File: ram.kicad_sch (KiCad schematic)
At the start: 36 parts, among them IC25 74LVC139, U2 TXS0108EPW, U3 TXS0108EPW, U4 TXS0108EPW, U5 TXS0108EPW, U6 IS41LV16105D, U7 IS41LV16105D, U8 TXS0108EPW, U9 TXS0108EPW

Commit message: revise for fabrication
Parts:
- added IC11, IC6: HM514260AJ8, Acorn:SOJ-42_10.16mm_P1.27mm, symbol Acorn:HYB5118165BSJ
- added RP2, RP4, RP5, RP6: 68R, Package_SO:SOIC-16W_5.3x10.2mm_P1.27mm, symbol Device:R_Pack08
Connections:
- net +3.3V: now also C152.1, C160.1, C163.1, C166.1, C2.1, C4.1; no longer C11.1, C12.1, C13.1, C131.1, C162.2, C17.1, C18.1, C19.1, C228.1, IC25.13 (A1), IC25.14 (A0), IC25.15 (E), IC25.16 (VCC), L15.1, L16.1, R136.1
- net +5V: now also C11.1, C12.1, C13.1, C131.1, C162.2, C17.1, C18.1, C19.1, C228.1, IC25.13 (A1), IC25.14 (A0), IC25.15 (E), IC25.16 (VCC), L15.1, L16.1, R136.1, IC11.1 (Vcc), IC11.21 (Vcc), IC11.6 (Vcc), IC6.1 (Vcc), IC6.21 (Vcc), IC6.6 (Vcc); no longer C152.1, C160.1, C163.1, C166.1, C2.1, C4.1
- net Cas0: now also IC6.31 (~{LCAS})
- net Cas1: now also IC6.30 (~{UCAS})
- net Cas2: now also IC11.31 (~{LCAS})
- net Cas3: now also IC11.30 (~{UCAS})
- net D0: now also RP2.1 (R1.1)
- net D1: now also RP2.2 (R2.1)
- net D10: now also RP4.6 (R6.1)
- net D11: now also RP4.5 (R5.1)
- net D12: now also RP4.4 (R4.1)
- net D13: now also RP4.3 (R3.1)
- net D14: now also RP4.2 (R2.1)
- net D15: now also RP4.1 (R1.1)
- net D16: now also RP5.8 (R8.1)
- net D17: now also RP5.7 (R7.1)
- net D18: now also RP5.6 (R6.1)
- net D19: now also RP5.5 (R5.1)
- net D2: now also RP2.3 (R3.1)
- net D20: now also RP5.4 (R4.1)
- net D21: now also RP5.3 (R3.1)
- net D22: now also RP5.2 (R2.1)
- net D23: now also RP5.1 (R1.1)
- net D24: now also RP6.4 (R4.1)
- net D25: now also RP6.3 (R3.1)
- net D26: now also RP6.2 (R2.1)
- net D27: now also RP6.1 (R1.1)
- net D28: now also RP6.5 (R5.1)
- net D29: now also RP6.6 (R6.1)
- net D3: now also RP2.4 (R4.1)
- net D30: now also RP6.7 (R7.1)
- net D31: now also RP6.8 (R8.1)
- net D4: now also RP2.5 (R5.1)
- net D5: now also RP2.6 (R6.1)
- net D6: now also RP2.7 (R7.1)
- net D7: now also RP2.8 (R8.1)
- net D8: now also RP4.8 (R8.1)
- net D9: now also RP4.7 (R7.1)
- net Dbe: now also IC25.2 (A0)
- net Dbe3: no longer IC25.2 (A0)
- net GND: now also IC11.22 (Vss), IC11.37 (Vss), IC11.42 (Vss), IC6.22 (Vss), IC6.37 (Vss), IC6.42 (Vss)
- net Ra0: now also IC11.17 (A0), IC6.17 (A0)
- net Ra1: now also IC11.18 (A1), IC6.18 (A1)
- net Ra2: now also IC11.19 (A2), IC6.19 (A2)
- net Ra3: now also IC11.20 (A3), IC6.20 (A3)
- net Ra4: now also IC11.23 (A4), IC6.23 (A4)
- net Ra5: now also IC11.24 (A5), IC6.24 (A5)
- net Ra6: now also IC11.25 (A6), IC6.25 (A6)
- net Ra7: now also IC11.26 (A7), IC6.26 (A7)
- net Ra8: now also IC11.27 (A8), IC6.27 (A8)
- net Ra9: now also IC11.28 (A9), IC6.28 (A9)
- net Rd0: now also IC6.2 (IO0), RP2.16 (R1.2)
- net Rd1: now also IC6.3 (IO1), RP2.15 (R2.2)
- net Rd10: now also IC6.35 (IO10), RP4.11 (R6.2)
- net Rd11: now also IC6.36 (IO11), RP4.12 (R5.2)
- net Rd12: now also IC6.38 (IO12), RP4.13 (R4.2)
- net Rd13: now also IC6.39 (IO13), RP4.14 (R3.2)
- net Rd14: now also IC6.40 (IO14), RP4.15 (R2.2)
- net Rd15: now also IC6.41 (IO15), RP4.16 (R1.2)
- net Rd16: now also IC11.2 (IO0), RP5.9 (R8.2)
- net Rd17: now also IC11.3 (IO1), RP5.10 (R7.2)
- net Rd18: now also IC11.4 (IO2), RP5.11 (R6.2)
- net Rd19: now also IC11.5 (IO3), RP5.12 (R5.2)
- net Rd2: now also IC6.4 (IO2), RP2.14 (R3.2)
- net Rd20: now also IC11.7 (IO4), RP5.13 (R4.2)
- net Rd21: now also IC11.8 (IO5), RP5.14 (R3.2)
- net Rd22: now also IC11.9 (IO6), RP5.15 (R2.2)
- net Rd23: now also IC11.10 (IO7), RP5.16 (R1.2)
- net Rd24: now also IC11.36 (IO11), RP6.13 (R4.2)
- net Rd25: now also IC11.35 (IO10), RP6.14 (R3.2)
- net Rd26: now also IC11.34 (IO9), RP6.15 (R2.2)
- net Rd27: now also IC11.33 (IO8), RP6.16 (R1.2)
- net Rd28: now also IC11.38 (IO12), RP6.12 (R5.2)
- net Rd29: now also IC11.39 (IO13), RP6.11 (R6.2)
- net Rd3: now also IC6.5 (IO3), RP2.13 (R4.2)
- net Rd30: now also IC11.40 (IO14), RP6.10 (R7.2)
- net Rd31: now also IC11.41 (IO15), RP6.9 (R8.2)
- net Rd4: now also IC6.7 (IO4), RP2.12 (R5.2)
- net Rd5: now also IC6.8 (IO5), RP2.11 (R6.2)
- net Rd6: now also IC6.9 (IO6), RP2.10 (R7.2)
- net Rd7: now also IC6.10 (IO7), RP2.9 (R8.2)
- net Rd8: now also IC6.33 (IO8), RP4.9 (R8.2)
- net Rd9: now also IC6.34 (IO9), RP4.10 (R7.2)
- net ~{OE2}: now also IC11.29 (~{OE}), IC6.29 (~{OE})
- net ~{Ras}: now also IC11.14 (~{RAS}), IC6.14 (~{RAS})
- net ~{WR2}: now also IC11.13 (~{WE}), IC6.13 (~{WE})
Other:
- moved on the sheet: U2, U3, U4, U5, U6, U7, U8, U9

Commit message: prepare for fabrication
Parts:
- C10, C11, C12, C13, C152, C160, C162, C163, C166, C17, C18, C19, C2, C4, C5, C6, C7, C8, C9: LCSC (none) -> C49678; LCSC Part (none) -> C49678
- IC25: LCSC (none) -> C7662; LCSC Part (none) -> C7662
- R135: LCSC (none) -> C17630; LCSC Part (none) -> C17630
- R136: LCSC (none) -> C2907219; LCSC Part (none) -> C2907219
- RP2, RP4, RP5, RP6: value 68R -> 68Rx8; LCSC (none) -> C1739978; LCSC Part (none) -> C1739978
- U2, U3, U4, U5, U8, U9: LCSC (none) -> C17206; LCSC Part (none) -> C17206
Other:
- moved on the sheet: RP2, RP4, RP5, RP6

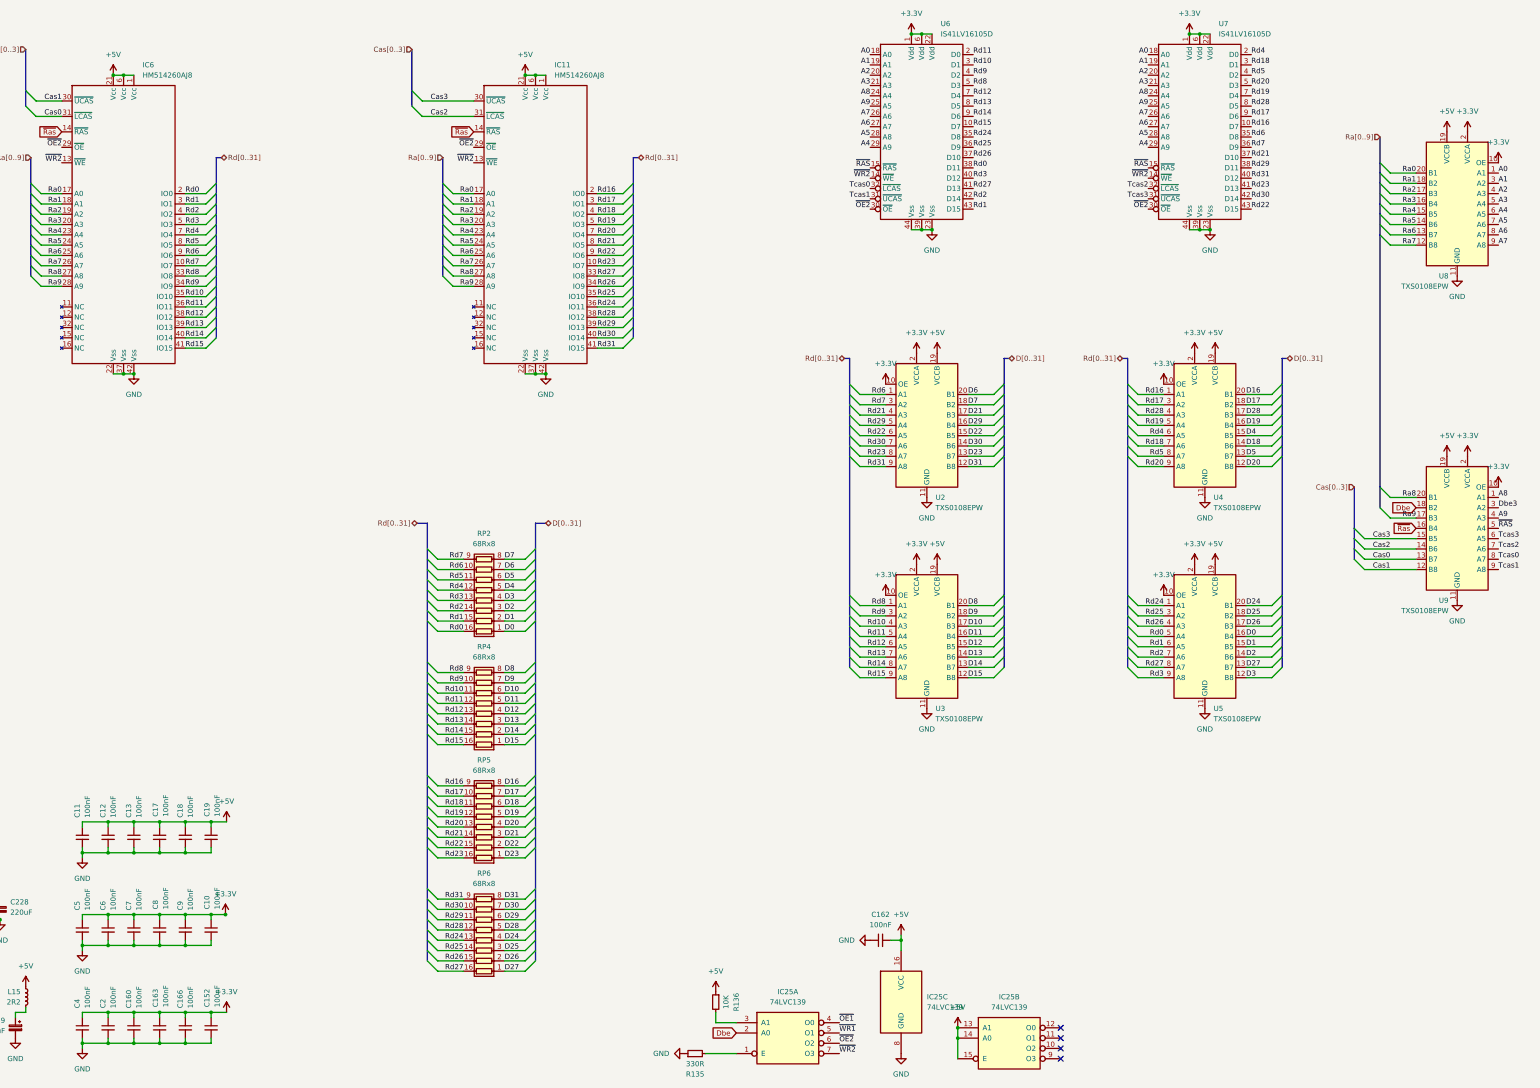
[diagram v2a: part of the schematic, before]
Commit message: fix CX1
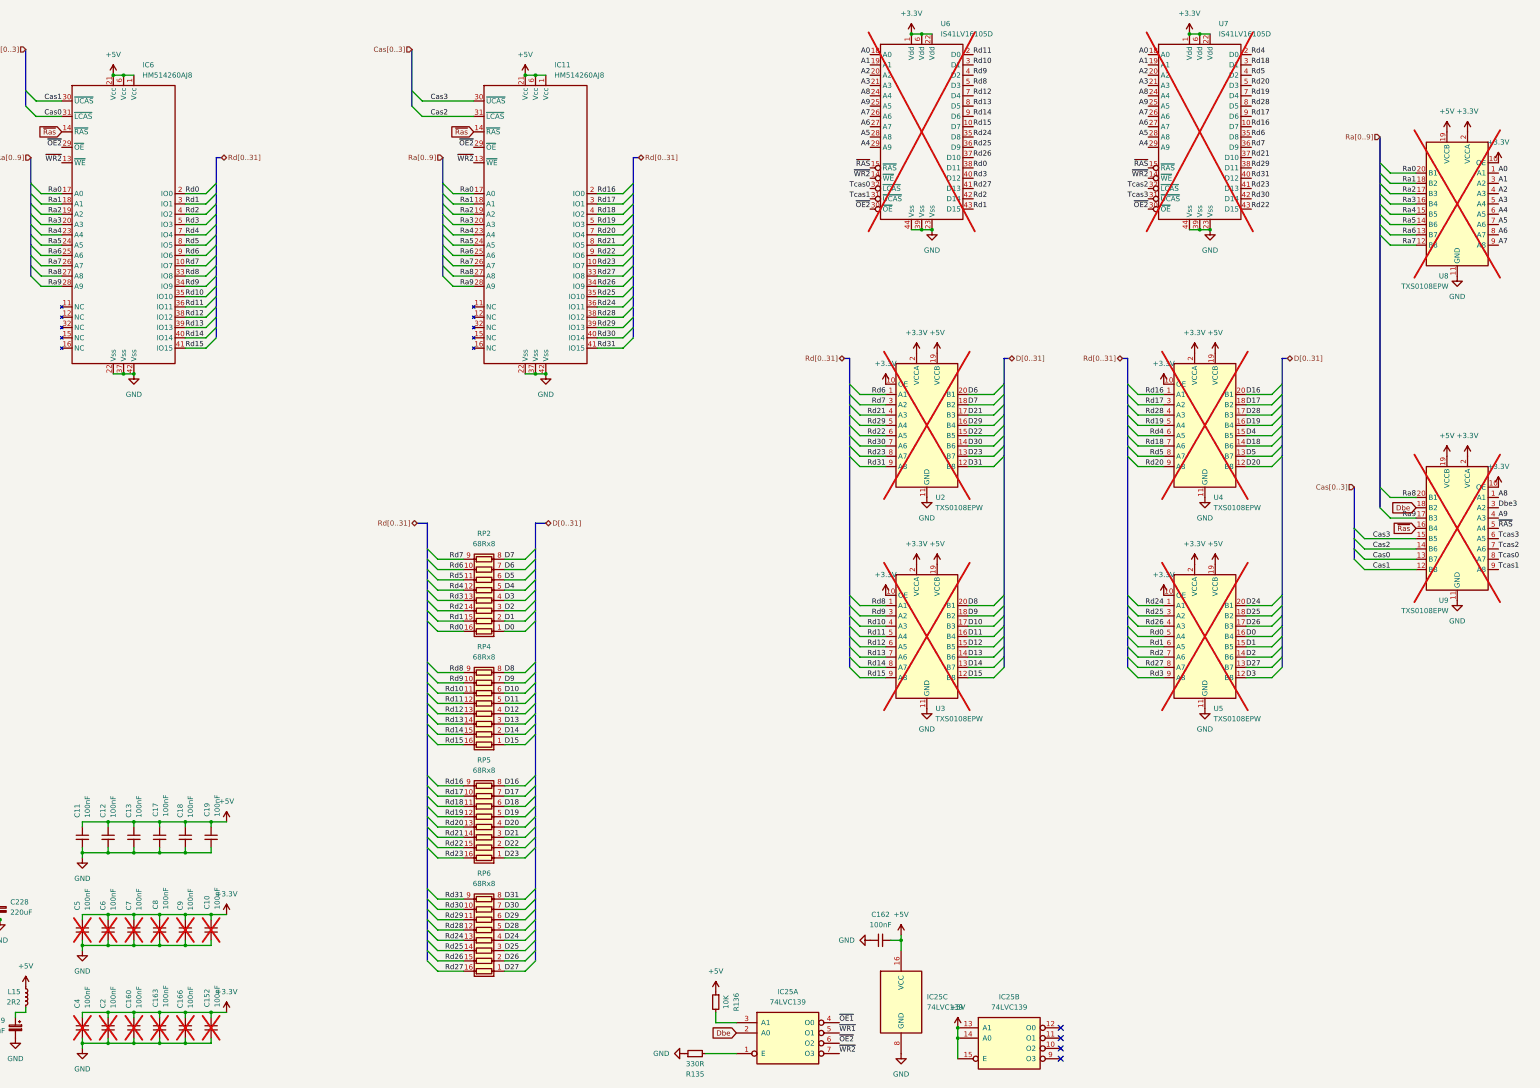
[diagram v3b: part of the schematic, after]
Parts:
- C10, C152, C160, C163, C166, C2, C4, C5, C6, C7, C8, C9, U2, U3, U4, U5, U6, U7, U8, U9: now not fitted; now left out of the parts list
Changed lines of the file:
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@@
 	)
 	(junction
-		(at 84.8234 238.76)
-		(diameter 0)
-		(color 0 0 0 0)
-	)
-	(junction
 		(at 256.54 21.59)
 		(diameter 0)
@@
 	(wire
 		(pts
-			(xy 81.28 238.76) (xy 84.8234 238.76)
+			(xy 81.28 238.76) (xy 85.09 238.76)
 		)
 		(stroke
@@
 	(wire
 		(pts
-			(xy 84.8234 238.76) (xy 85.09 238.76)
-		)
-		(stroke
-			(width 0)
-			(type default)
-		)
-	)
-	(wire
-		(pts
 			(xy 241.3 123.19) (xy 247.65 123.19)
 		)
@@
 		(unit 1)
 		(exclude_from_sim no)
-		(in_bom yes)
+		(in_bom no)
 		(on_board no)
-		(dnp no)
+		(dnp yes)
 		(property "Reference" "C4"
 			(at 48.26 261.874 90)
@@
 		(unit 1)
 		(exclude_from_sim no)
-		(in_bom yes)
+		(in_bom no)
 		(on_board no)
-		(dnp no)
+		(dnp yes)
 		(fields_autoplaced yes)
 		(property "Reference" "U7"
@@
 		(unit 1)
 		(exclude_from_sim no)
-		(in_bom yes)
+		(in_bom no)
 		(on_board no)
-		(dnp no)
+		(dnp yes)
 		(property "Reference" "C5"
 			(at 48.26 237.744 90)
@@
 		(unit 1)
 		(exclude_from_sim no)
-		(in_bom yes)
+		(in_bom no)
 		(on_board no)
-		(dnp no)
+		(dnp yes)
 		(property "Reference" "C152"
 			(at 80.264 261.62 90)
@@
 		(unit 1)
 		(exclude_from_sim no)
-		(in_bom yes)
+		(in_bom no)
 		(on_board no)
-		(dnp no)
+		(dnp yes)
 		(property "Reference" "C10"
 			(at 80.264 237.49 90)
@@
 		(unit 1)
 		(exclude_from_sim no)
-		(in_bom yes)
+		(in_bom no)
 		(on_board no)
-		(dnp no)
+		(dnp yes)
 		(property "Reference" "C6"
 			(at 54.61 237.744 90)
@@
 		(unit 1)
 		(exclude_from_sim no)
-		(in_bom yes)
+		(in_bom no)
 		(on_board no)
-		(dnp no)
+		(dnp yes)
 		(property "Reference" "C163"
 			(at 67.564 261.62 90)
@@
 		(unit 1)
 		(exclude_from_sim no)
-		(in_bom yes)
+		(in_bom no)
 		(on_board no)
-		(dnp no)
+		(dnp yes)
 		(fields_autoplaced yes)
 		(property "Reference" "U8"
@@
 		(unit 1)
 		(exclude_from_sim no)
-		(in_bom yes)
+		(in_bom no)
 		(on_board no)
-		(dnp no)
+		(dnp yes)
 		(fields_autoplaced yes)
 		(property "Reference" "U9"
@@
 		(unit 1)
 		(exclude_from_sim no)
-		(in_bom yes)
+		(in_bom no)
 		(on_board no)
-		(dnp no)
+		(dnp yes)
 		(fields_autoplaced yes)
 		(property "Reference" "U6"
@@
 		(unit 1)
 		(exclude_from_sim no)
-		(in_bom yes)
+		(in_bom no)
 		(on_board no)
-		(dnp no)
+		(dnp yes)
 		(fields_autoplaced yes)
 		(property "Reference" "U3"
@@
 		(unit 1)
 		(exclude_from_sim no)
-		(in_bom yes)
+		(in_bom no)
 		(on_board no)
-		(dnp no)
+		(dnp yes)
 		(property "Reference" "C160"
 			(at 60.96 261.874 90)
@@
 		(unit 1)
 		(exclude_from_sim no)
-		(in_bom yes)
+		(in_bom no)
 		(on_board no)
-		(dnp no)
+		(dnp yes)
 		(property "Reference" "C166"
 			(at 73.66 261.874 90)
@@
 		(unit 1)
 		(exclude_from_sim no)
-		(in_bom yes)
+		(in_bom no)
 		(on_board no)
-		(dnp no)
+		(dnp yes)
 		(fields_autoplaced yes)
 		(property "Reference" "U5"
@@
 		(unit 1)
 		(exclude_from_sim no)
-		(in_bom yes)
+		(in_bom no)
 		(on_board no)
-		(dnp no)
+		(dnp yes)
 		(fields_autoplaced yes)
 		(property "Reference" "U2"
@@
 		(unit 1)
 		(exclude_from_sim no)
-		(in_bom yes)
+		(in_bom no)
 		(on_board no)
-		(dnp no)
+		(dnp yes)
 		(fields_autoplaced yes)
 		(property "Reference" "U4"
@@
 		(unit 1)
 		(exclude_from_sim no)
-		(in_bom yes)
+		(in_bom no)
 		(on_board no)
-		(dnp no)
+		(dnp yes)
 		(property "Reference" "C2"
 			(at 54.61 261.874 90)
@@
 	(symbol
 		(lib_id "power:+3.3V")
-		(at 84.8234 238.76 0)
+		(at 85.09 238.76 0)
 		(unit 1)
 		(exclude_from_sim no)
@@
 		(fields_autoplaced yes)
 		(property "Reference" "#PWR019"
-			(at 84.8234 242.57 0)
+			(at 85.09 242.57 0)
 			(effects
 				(font
@@
 		)
 		(property "Value" "+3.3V"
-			(at 84.8234 233.68 0)
+			(at 85.09 233.68 0)
 			(effects
 				(font
@@
 		)
 		(property "Footprint" ""
-			(at 84.8234 238.76 0)
+			(at 85.09 238.76 0)
 			(effects
 				(font
@@
 		)
 		(property "Datasheet" ""
-			(at 84.8234 238.76 0)
+			(at 85.09 238.76 0)
 			(effects
 				(font
@@
 		)
 		(property "Description" "Power symbol creates a global label with name \"+3.3V\""
-			(at 84.8234 238.76 0)
+			(at 85.09 238.76 0)
 			(effects
 				(font
@@
 		(unit 1)
 		(exclude_from_sim no)
-		(in_bom yes)
+		(in_bom no)
 		(on_board no)
-		(dnp no)
+		(dnp yes)
 		(property "Reference" "C8"
 			(at 67.564 237.49 90)
@@
 		(unit 1)
 		(exclude_from_sim no)
-		(in_bom yes)
+		(in_bom no)
 		(on_board no)
-		(dnp no)
+		(dnp yes)
 		(property "Reference" "C9"
 			(at 73.66 237.744 90)
@@
 		(unit 1)
 		(exclude_from_sim no)
-		(in_bom yes)
+		(in_bom no)
 		(on_board no)
-		(dnp no)
+		(dnp yes)
 		(property "Reference" "C7"
 			(at 60.96 237.744 90)

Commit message: update design to correct errors found by IanJ
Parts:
- IC25: value 74LVC139 -> 74ALS139; footprint Package_SO:TSSOP-16_4.4x5mm_P0.65mm -> Package_SO:SOIC-16_3.9x9.9mm_P1.27mm; LCSC C7662 -> (none); LCSC Part C7662 -> (none)
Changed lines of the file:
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@@
 			)
 		)
-		(property "Value" "74LVC139"
+		(property "Value" "74ALS139"
 			(at 223.52 260.35 0)
 			(effects
@@
 			)
 		)
-		(property "Footprint" "Package_SO:TSSOP-16_4.4x5mm_P0.65mm"
+		(property "Footprint" "Package_SO:SOIC-16_3.9x9.9mm_P1.27mm"
 			(at 223.52 267.97 0)
 			(effects
@@
 			)
 		)
-		(property "LCSC" "C7662"
+		(property "LCSC" ""
 			(at 223.52 267.97 0)
 			(effects
@@
 			)
 		)
-		(property "LCSC Part" "C7662"
+		(property "LCSC Part" ""
 			(at 223.52 267.97 0)
 			(effects
@@
 			)
 		)
-		(property "Value" "74LVC139"
+		(property "Value" "74ALS139"
 			(at 257.81 261.6199 0)
 			(effects
@@
 			)
 		)
-		(property "Footprint" "Package_SO:TSSOP-16_4.4x5mm_P0.65mm"
+		(property "Footprint" "Package_SO:SOIC-16_3.9x9.9mm_P1.27mm"
 			(at 251.46 260.35 0)
 			(effects
@@
 			)
 		)
-		(property "LCSC" "C7662"
+		(property "LCSC" ""
 			(at 251.46 260.35 0)
 			(effects
@@
 			)
 		)
-		(property "LCSC Part" "C7662"
+		(property "LCSC Part" ""
 			(at 251.46 260.35 0)
 			(effects
@@
 			)
 		)
-		(property "Value" "74LVC139"
+		(property "Value" "74ALS139"
 			(at 278.13 261.62 0)
 			(effects
@@
 			)
 		)
-		(property "Footprint" "Package_SO:TSSOP-16_4.4x5mm_P0.65mm"
+		(property "Footprint" "Package_SO:SOIC-16_3.9x9.9mm_P1.27mm"
 			(at 278.13 269.24 0)
 			(effects
@@
 			)
 		)
-		(property "LCSC" "C7662"
+		(property "LCSC" ""
 			(at 278.13 269.24 0)
 			(effects
@@
 			)
 		)
-		(property "LCSC Part" "C7662"
+		(property "LCSC Part" ""
 			(at 278.13 269.24 0)
 			(effects

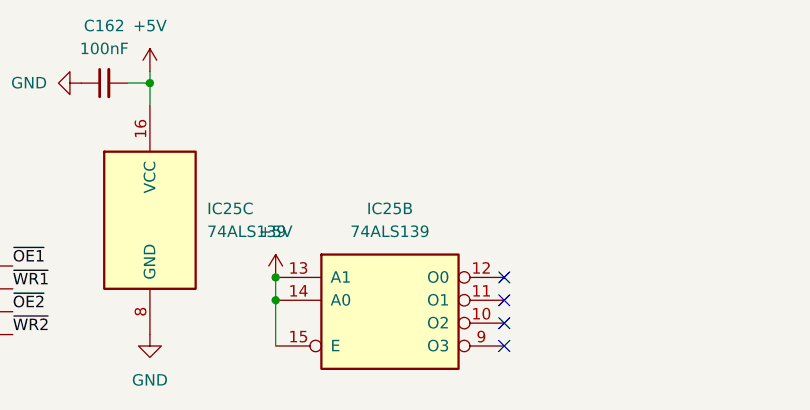
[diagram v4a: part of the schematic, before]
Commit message: move RP11 inline instead of pullup
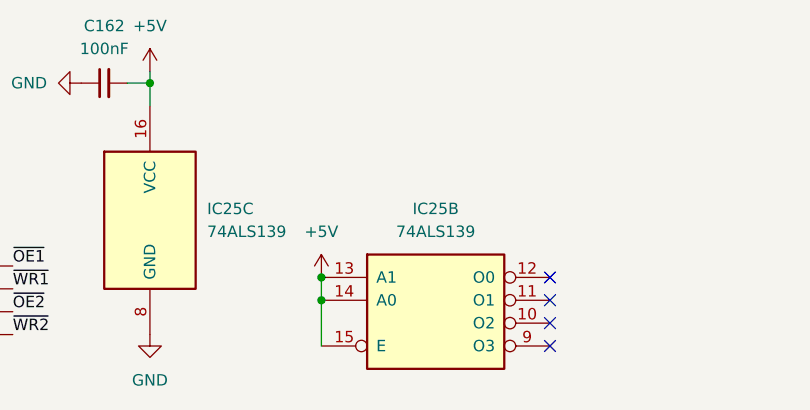
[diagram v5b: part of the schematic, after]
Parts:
- IC25: LCSC (none) -> C7494; LCSC Part (none) -> C7494
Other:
- moved on the sheet: IC25B
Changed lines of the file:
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@@
 	)
 	(junction
-		(at 265.43 266.7)
+		(at 270.51 266.7)
 		(diameter 0)
 		(color 0 0 0 0)
@@
 	)
 	(junction
-		(at 265.43 269.24)
+		(at 270.51 269.24)
 		(diameter 0)
 		(color 0 0 0 0)
@@
 	)
 	(no_connect
-		(at 290.83 269.24)
+		(at 295.91 269.24)
 	)
 	(no_connect
-		(at 290.83 271.78)
+		(at 295.91 271.78)
 	)
 	(no_connect
-		(at 290.83 274.32)
+		(at 295.91 274.32)
 	)
 	(no_connect
-		(at 290.83 266.7)
+		(at 295.91 266.7)
 	)
 	(bus_entry
@@
 	(wire
 		(pts
-			(xy 265.43 266.7) (xy 265.43 269.24)
+			(xy 270.51 266.7) (xy 270.51 269.24)
 		)
 		(stroke
@@
 	(wire
 		(pts
-			(xy 265.43 269.24) (xy 265.43 274.32)
+			(xy 270.51 269.24) (xy 270.51 274.32)
 		)
 		(stroke
@@
 			)
 		)
-		(property "LCSC" ""
+		(property "LCSC" "C7494"
 			(at 223.52 267.97 0)
 			(effects
@@
 			)
 		)
-		(property "LCSC Part" ""
+		(property "LCSC Part" "C7494"
 			(at 223.52 267.97 0)
 			(effects
@@
 			)
 		)
-		(property "LCSC" ""
+		(property "LCSC" "C7494"
 			(at 251.46 260.35 0)
 			(effects
@@
 			)
 		)
-		(property "LCSC Part" ""
+		(property "LCSC Part" "C7494"
 			(at 251.46 260.35 0)
 			(effects
@@
 	(symbol
 		(lib_id "power:+5V")
-		(at 265.43 266.7 0)
+		(at 270.51 266.7 0)
 		(unit 1)
 		(exclude_from_sim no)
@@
 		(fields_autoplaced yes)
 		(property "Reference" "#PWR014"
-			(at 265.43 270.51 0)
+			(at 270.51 270.51 0)
 			(effects
 				(font
@@
 		)
 		(property "Value" "+5V"
-			(at 265.43 261.62 0)
+			(at 270.51 261.62 0)
 			(effects
 				(font
@@
 		)
 		(property "Footprint" ""
-			(at 265.43 266.7 0)
+			(at 270.51 266.7 0)
 			(effects
 				(font
@@
 		)
 		(property "Datasheet" ""
-			(at 265.43 266.7 0)
+			(at 270.51 266.7 0)
 			(effects
 				(font
@@
 		)
 		(property "Description" "Power symbol creates a global label with name \"+5V\""
-			(at 265.43 266.7 0)
+			(at 270.51 266.7 0)
 			(effects
 				(font
@@
 	(symbol
 		(lib_id "74xx:74LS139")
-		(at 278.13 269.24 0)
+		(at 283.21 269.24 0)
 		(unit 2)
 		(exclude_from_sim no)
@@
 		(fields_autoplaced yes)
 		(property "Reference" "IC25"
-			(at 278.13 259.08 0)
+			(at 283.21 259.08 0)
 			(effects
 				(font
@@
 		)
 		(property "Value" "74ALS139"
-			(at 278.13 261.62 0)
+			(at 283.21 261.62 0)
 			(effects
 				(font
@@
 		)
 		(property "Footprint" "Package_SO:SOIC-16_3.9x9.9mm_P1.27mm"
-			(at 278.13 269.24 0)
+			(at 283.21 269.24 0)
 			(effects
 				(font
@@
 		)
 		(property "Datasheet" "http://www.ti.com/lit/ds/symlink/sn74ls139a.pdf"
-			(at 278.13 269.24 0)
+			(at 283.21 269.24 0)
 			(effects
 				(font
@@
 		)
 		(property "Description" "Dual Decoder 1 of 4, Active low outputs"
-			(at 278.13 269.24 0)
+			(at 283.21 269.24 0)
 			(effects
 				(font
@@
 			)
 		)
-		(property "LCSC" ""
-			(at 278.13 269.24 0)
+		(property "LCSC" "C7494"
+			(at 283.21 269.24 0)
 			(effects
 				(font
@@
 			)
 		)
-		(property "LCSC Part" ""
-			(at 278.13 269.24 0)
+		(property "LCSC Part" "C7494"
+			(at 283.21 269.24 0)
 			(effects
 				(font
